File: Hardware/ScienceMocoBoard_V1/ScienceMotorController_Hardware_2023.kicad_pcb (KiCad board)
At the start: 2 copper layers, 127 x 124.6 mm, 140 parts, among them Q1 SI4156DY, Q10 SI4156DY, Q11 SI4156DY, Q12 SI4156DY, Q13 SI4156DY, Q14 SI4156DY, Q15 SI4156DY, Q16 SI4156DY, Q2 SI4156DY, Q3 SI4156DY, Q4 SI4156DY, Q5 SI4156DY, Q6 SI4156DY, Q7 SI4156DY, Q8 SI4156DY, Q9 SI4156DY, U1 IRS2005S, U10 IRS2005S, U11 TM4C129E_Launchpad, U2 IRS2005S, U3 3V3 OKI, U4 TSR_1-2450, U5 IRS2005S, U6 IRS2005S, U7 IRS2005S, U8 IRS2005S, U9 IRS2005S

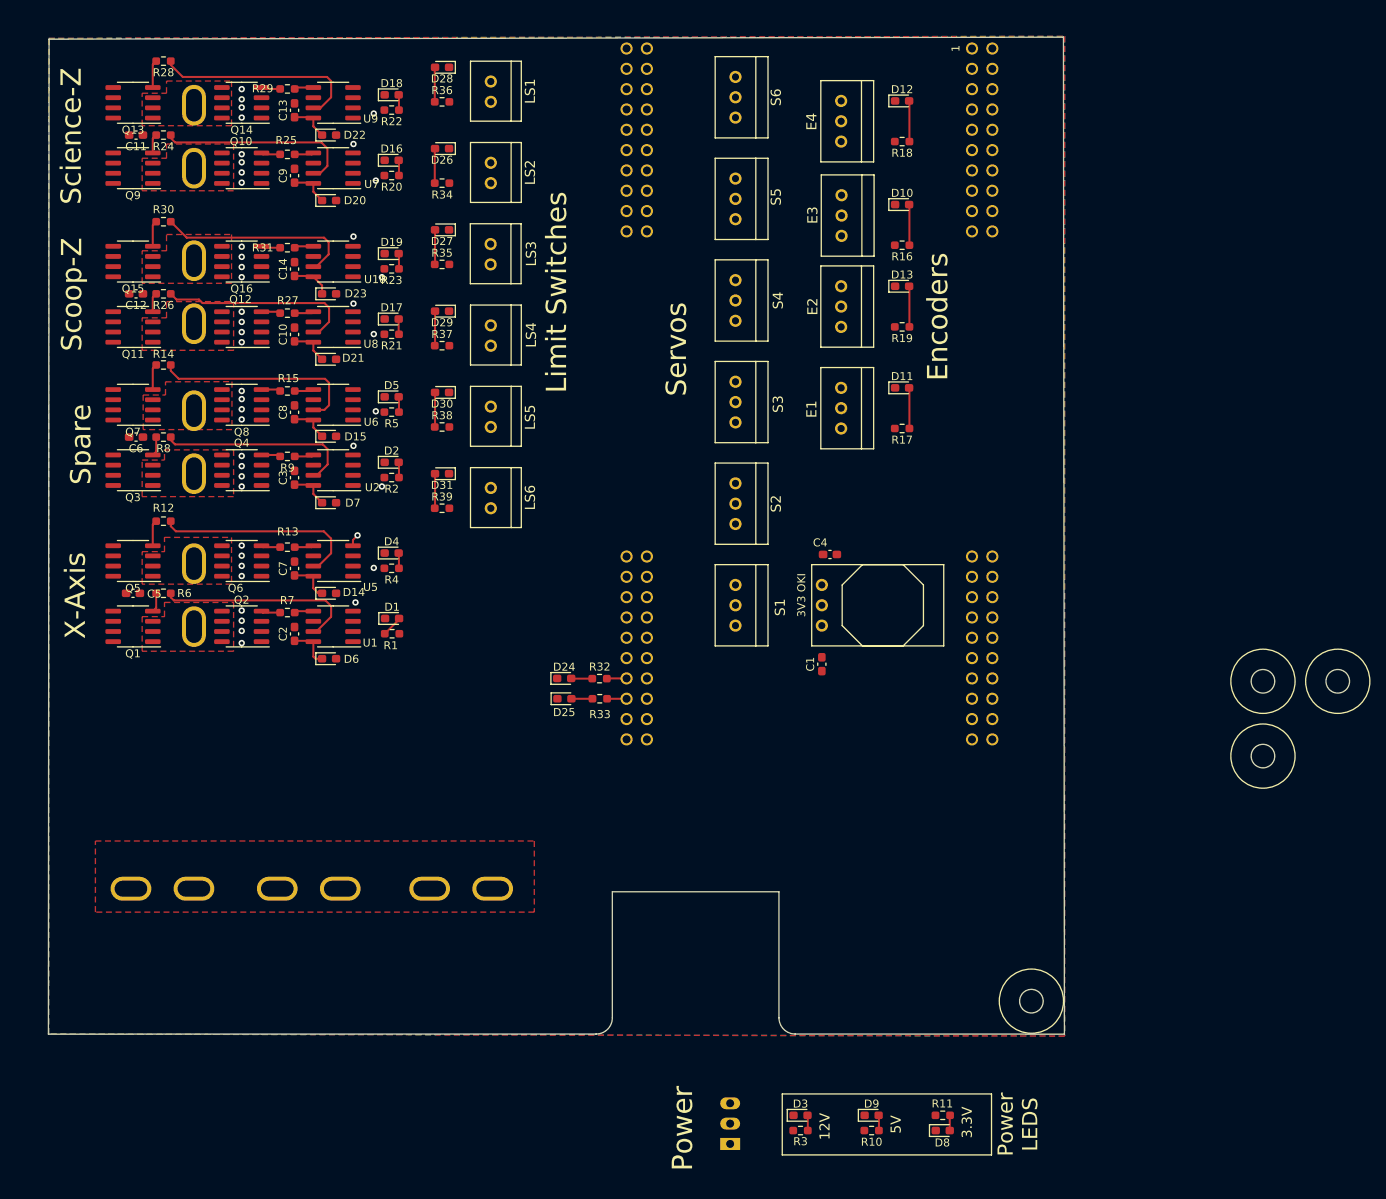
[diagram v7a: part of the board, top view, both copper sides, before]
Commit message: 12V plane made. Started Traces.
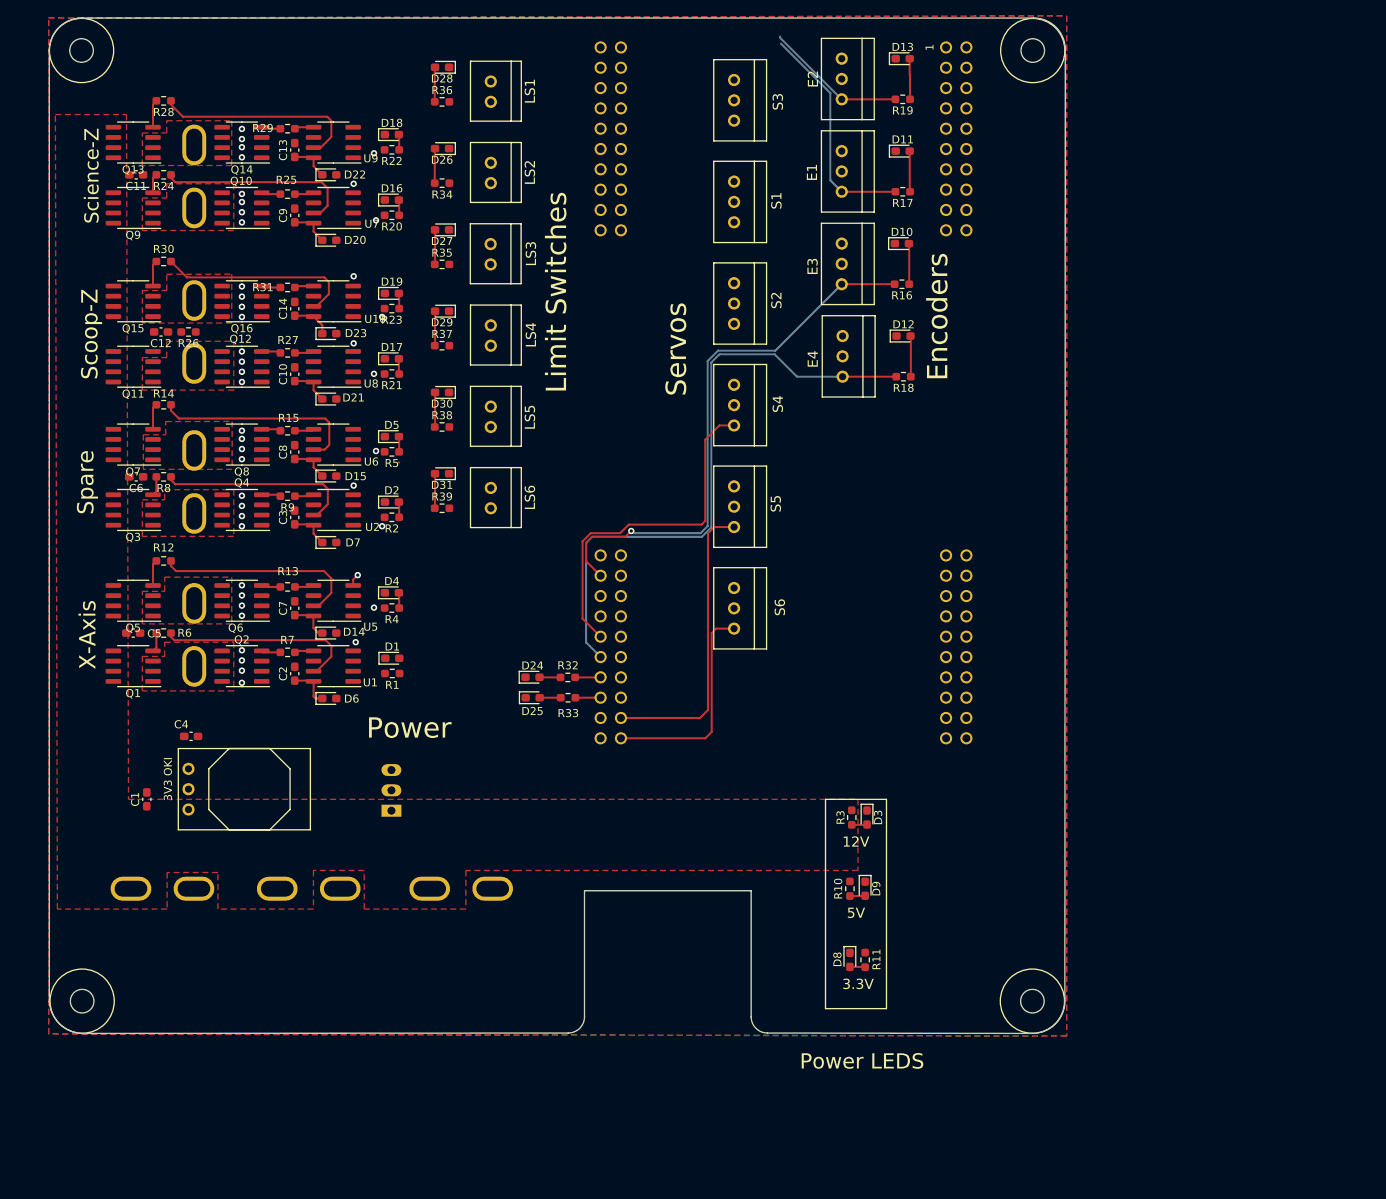
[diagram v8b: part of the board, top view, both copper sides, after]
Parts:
- moved V2 168.6 mm to (46.1, 38.9), turned to 90 degrees
- moved V1 141.4 mm to (46.2, 149.7), turned to 180 degrees
- moved C1 86.1 mm to (50.3, 128.5)
- moved V4 83.9 mm to (157.0, 38.9)
- moved C4 83.0 mm to (55.8, 120.7)
- moved U3 82.4 mm to (55.5, 129.8)
- moved U4 59.4 mm to (80.9, 129.9)
- moved R3 39.6 mm to (138.4, 130.8), turned to 90 degrees
- moved D3 38.1 mm to (140.3, 130.8), turned to -90 degrees
- moved R10 30.3 mm to (138.2, 139.7), turned to 90 degrees
- moved AbsEncode1 29.6 mm to (137.2, 47.5)
- moved D11 29.6 mm to (144.8, 47.5)
- moved R17 29.6 mm to (144.8, 52.6)
- moved AbsEncode2 29.4 mm to (137.3, 70.6)
- moved D12 29.4 mm to (144.9, 70.6)
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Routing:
- net Encoder_PWM_3: track 0.00 -> 76.8 mm
- net Encoder_PWM_2: track 0.00 -> 69.1 mm, vias 0 -> 1
- net Servo_4: track 0.00 -> 43.7 mm
- net Servo_5: track 0.00 -> 37.0 mm
- net Encoder_PWM_1: track 0.00 -> 28.4 mm
- net Servo_6: track 0.00 -> 27.0 mm
- net Net-(R26-Pad1): track 24.8 -> 0.00 mm
- net Encoder_PWM_4: track 0.00 -> 17.8 mm
- net Net-(D1-Pad2): track 2.65 -> 0.00 mm
- net Net-(Q11-Pad4): track 2.41 -> 0.00 mm
- net Net-(R28-Pad1): track 26.2 -> 24.8 mm
- net Net-(Q13-Pad4): track 3.48 -> 2.88 mm
- net GND: track 2.07 -> 1.53 mm
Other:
- board size 127 x 124.6 mm -> 127 x 126.9 mm
